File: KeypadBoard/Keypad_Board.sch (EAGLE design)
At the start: 34 parts, among them Q1 4.3A/20V/54mΩ, U1 ESP32-WROOM-32E_(16MB), U2 LTC1730ES8-4.2#TRPBF

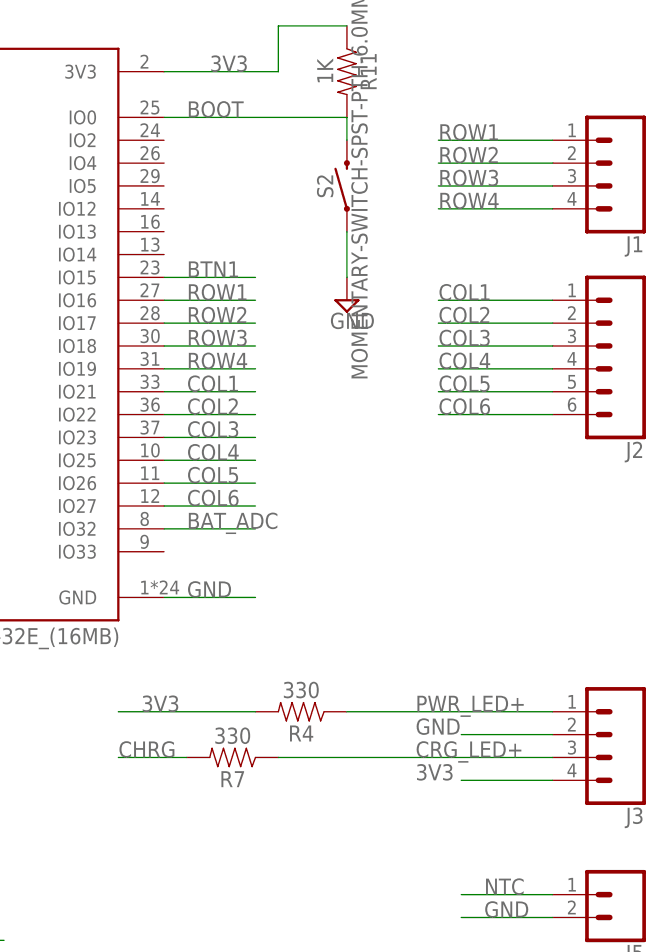
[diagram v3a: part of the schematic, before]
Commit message: Updated board for connection of a Micro SD Card module
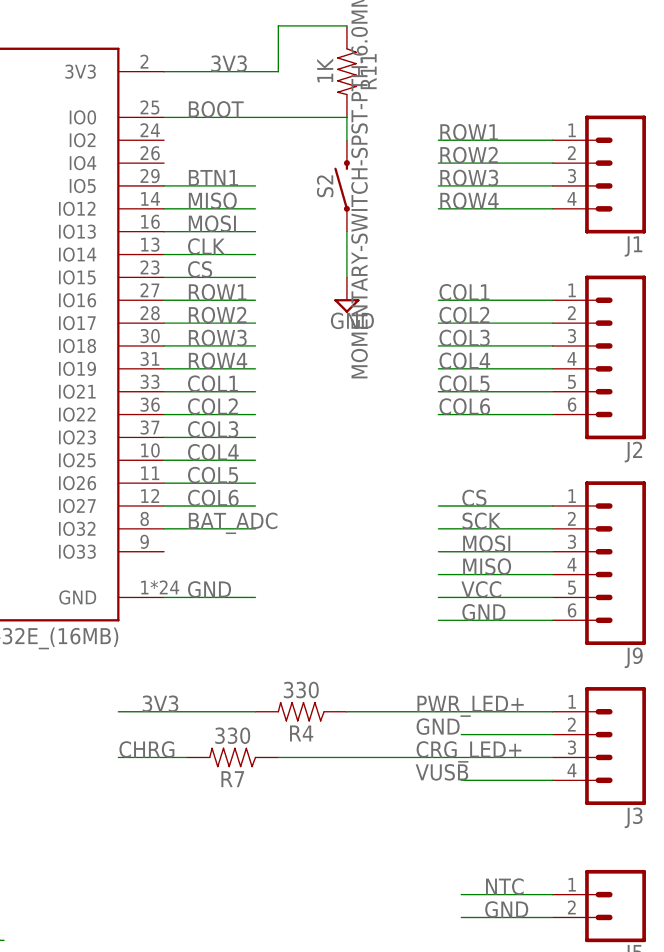
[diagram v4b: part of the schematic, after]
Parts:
- added J9: (no value), SparkFun-Connectors:CONN_06LOCK
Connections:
- new net CLK: U1.IO14
- new net CS: J9.1, U1.IO15
- new net MISO: J9.4, U1.IO12
- new net MOSI: J9.3, U1.IO13
- new net SCK: J9.2
- net 3V3: no longer J3.4
- net BTN1: now also U1.IO5; no longer U1.IO15
- net GND: now also J9.6
- net VCC: now also J9.5
- net VUSB: now also J3.4
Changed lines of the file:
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@@
 <part name="R13" library="SparkFun-Resistors" library_urn="urn:adsk.eagle:library:532" deviceset="0.22OHM" device="-0805-1/4W-1%" package3d_urn="urn:adsk.eagle:package:39651/1" value="120K"/>
 <part name="SUPPLY11" library="supply2" library_urn="urn:adsk.eagle:library:372" deviceset="GND" device=""/>
+<part name="J9" library="SparkFun-Connectors" library_urn="urn:adsk.eagle:library:513" deviceset="CONN_06" device="LOCK" package3d_urn="urn:adsk.eagle:package:38002/1"/>
 </parts>
 <sheets>
@@
 <attribute name="VALUE" x="112.395" y="90.805" size="1.778" layer="96"/>
 </instance>
+<instance part="J9" gate="G$1" x="322.58" y="101.6" smashed="yes" rot="R180">
+<attribute name="VALUE" x="327.66" y="111.506" size="1.778" layer="96" font="vector" rot="R180"/>
+<attribute name="NAME" x="327.66" y="90.932" size="1.778" layer="95" font="vector" rot="R180"/>
+</instance>
 </instances>
 <busses>
@@
 <pinref part="R12" gate="G$1" pin="2"/>
 <wire x1="114.3" y1="96.52" x2="114.3" y2="99.06" width="0.1524" layer="91"/>
+</segment>
+<segment>
+<pinref part="J9" gate="G$1" pin="6"/>
+<wire x1="317.5" y1="93.98" x2="304.8" y2="93.98" width="0.1524" layer="91"/>
+<label x="307.34" y="93.98" size="1.778" layer="95"/>
 </segment>
 </net>
@@
 <wire x1="76.2" y1="99.06" x2="88.9" y2="99.06" width="0.1524" layer="91"/>
 <label x="81.28" y="99.06" size="1.778" layer="95"/>
+</segment>
+<segment>
+<pinref part="J9" gate="G$1" pin="5"/>
+<wire x1="317.5" y1="96.52" x2="304.8" y2="96.52" width="0.1524" layer="91"/>
+<label x="307.34" y="96.52" size="1.778" layer="95"/>
 </segment>
 </net>
@@
 <label x="81.28" y="129.54" size="1.778" layer="95"/>
 </segment>
+<segment>
+<pinref part="J3" gate="G$1" pin="4"/>
+<wire x1="317.5" y1="76.2" x2="307.34" y2="76.2" width="0.1524" layer="91"/>
+<label x="302.26" y="76.2" size="1.778" layer="95"/>
+</segment>
 </net>
 <net name="3V3" class="0">
@@
 <label x="307.34" y="50.8" size="1.778" layer="95"/>
 </segment>
-<segment>
-<pinref part="J3" gate="G$1" pin="4"/>
-<wire x1="317.5" y1="76.2" x2="307.34" y2="76.2" width="0.1524" layer="91"/>
-<label x="302.26" y="76.2" size="1.778" layer="95"/>
-</segment>
 </net>
 <net name="N$9" class="0">
@@
 </segment>
 <segment>
-<pinref part="U1" gate="G$1" pin="IO15"/>
-<wire x1="274.32" y1="132.08" x2="284.48" y2="132.08" width="0.1524" layer="91"/>
-<label x="276.86" y="132.08" size="1.778" layer="95"/>
+<pinref part="U1" gate="G$1" pin="IO5"/>
+<wire x1="274.32" y1="142.24" x2="284.48" y2="142.24" width="0.1524" layer="91"/>
+<label x="276.86" y="142.24" size="1.778" layer="95"/>
 </segment>
 </net>
@@
 </segment>
 </net>
+<net name="MISO" class="0">
+<segment>
+<pinref part="U1" gate="G$1" pin="IO12"/>
+<wire x1="274.32" y1="139.7" x2="284.48" y2="139.7" width="0.1524" layer="91"/>
+<label x="276.86" y="139.7" size="1.778" layer="95"/>
+</segment>
+<segment>
+<pinref part="J9" gate="G$1" pin="4"/>
+<wire x1="317.5" y1="99.06" x2="304.8" y2="99.06" width="0.1524" layer="91"/>
+<label x="307.34" y="99.06" size="1.778" layer="95"/>
+</segment>
+</net>
+<net name="MOSI" class="0">
+<segment>
+<pinref part="U1" gate="G$1" pin="IO13"/>
+<wire x1="274.32" y1="137.16" x2="284.48" y2="137.16" width="0.1524" layer="91"/>
+<label x="276.86" y="137.16" size="1.778" layer="95"/>
+</segment>
+<segment>
+<pinref part="J9" gate="G$1" pin="3"/>
+<wire x1="317.5" y1="101.6" x2="304.8" y2="101.6" width="0.1524" layer="91"/>
+<label x="307.34" y="101.6" size="1.778" layer="95"/>
+</segment>
+</net>
+<net name="CLK" class="0">
+<segment>
+<pinref part="U1" gate="G$1" pin="IO14"/>
+<wire x1="274.32" y1="134.62" x2="284.48" y2="134.62" width="0.1524" layer="91"/>
+<label x="276.86" y="134.62" size="1.778" layer="95"/>
+</segment>
+</net>
+<net name="CS" class="0">
+<segment>
+<pinref part="U1" gate="G$1" pin="IO15"/>
+<wire x1="274.32" y1="132.08" x2="284.48" y2="132.08" width="0.1524" layer="91"/>
+<label x="276.86" y="132.08" size="1.778" layer="95"/>
+</segment>
+<segment>
+<pinref part="J9" gate="G$1" pin="1"/>
+<wire x1="317.5" y1="106.68" x2="304.8" y2="106.68" width="0.1524" layer="91"/>
+<label x="307.34" y="106.68" size="1.778" layer="95"/>
+</segment>
+</net>
+<net name="SCK" class="0">
+<segment>
+<pinref part="J9" gate="G$1" pin="2"/>
+<wire x1="317.5" y1="104.14" x2="304.8" y2="104.14" width="0.1524" layer="91"/>
+<label x="307.34" y="104.14" size="1.778" layer="95"/>
+</segment>
+</net>

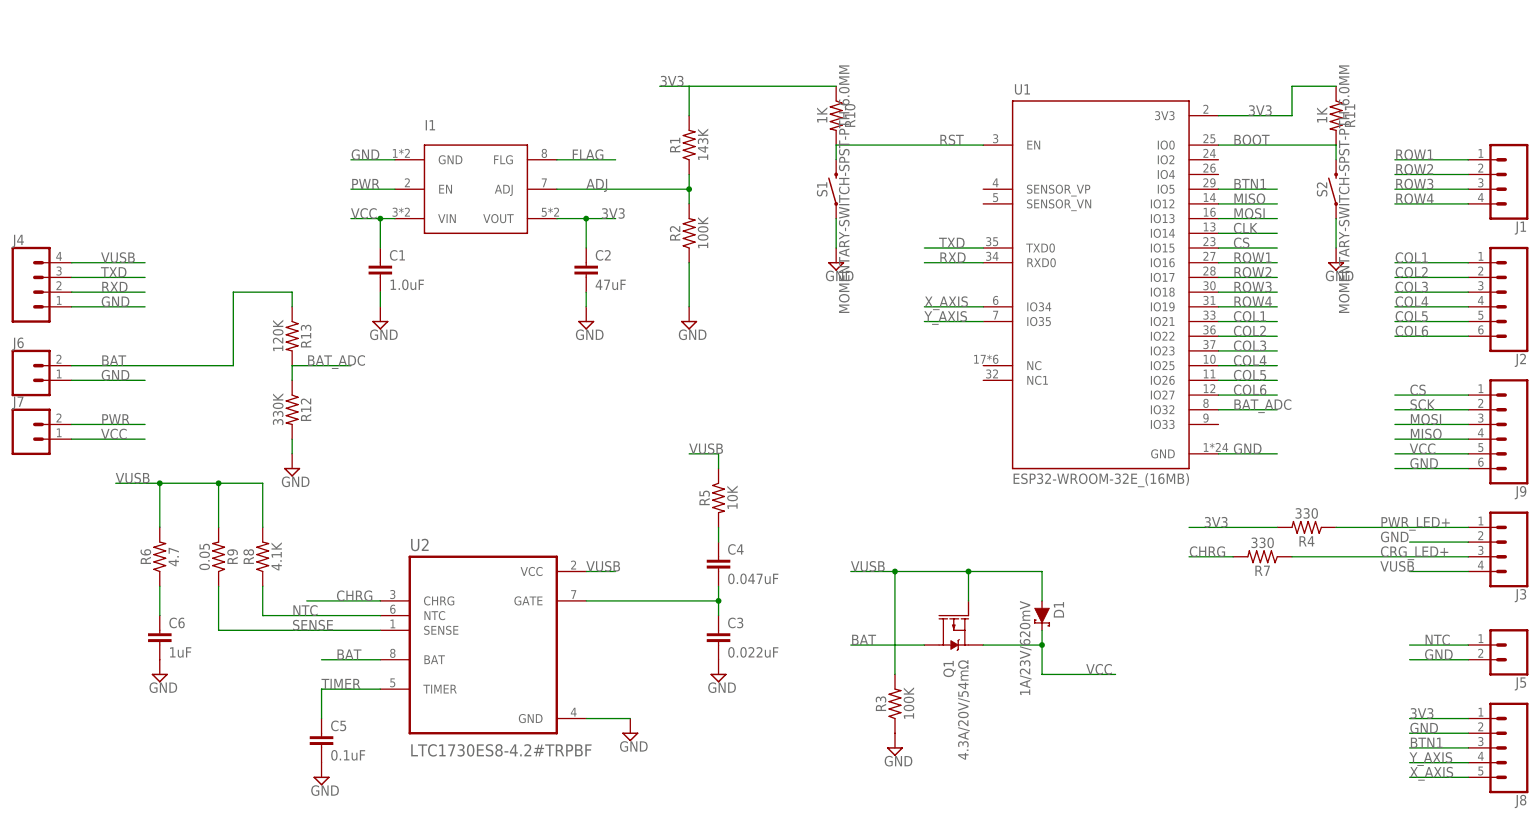
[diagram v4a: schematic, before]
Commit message: Board V4 - integrated battery holder, SD Breakout, mode LED's
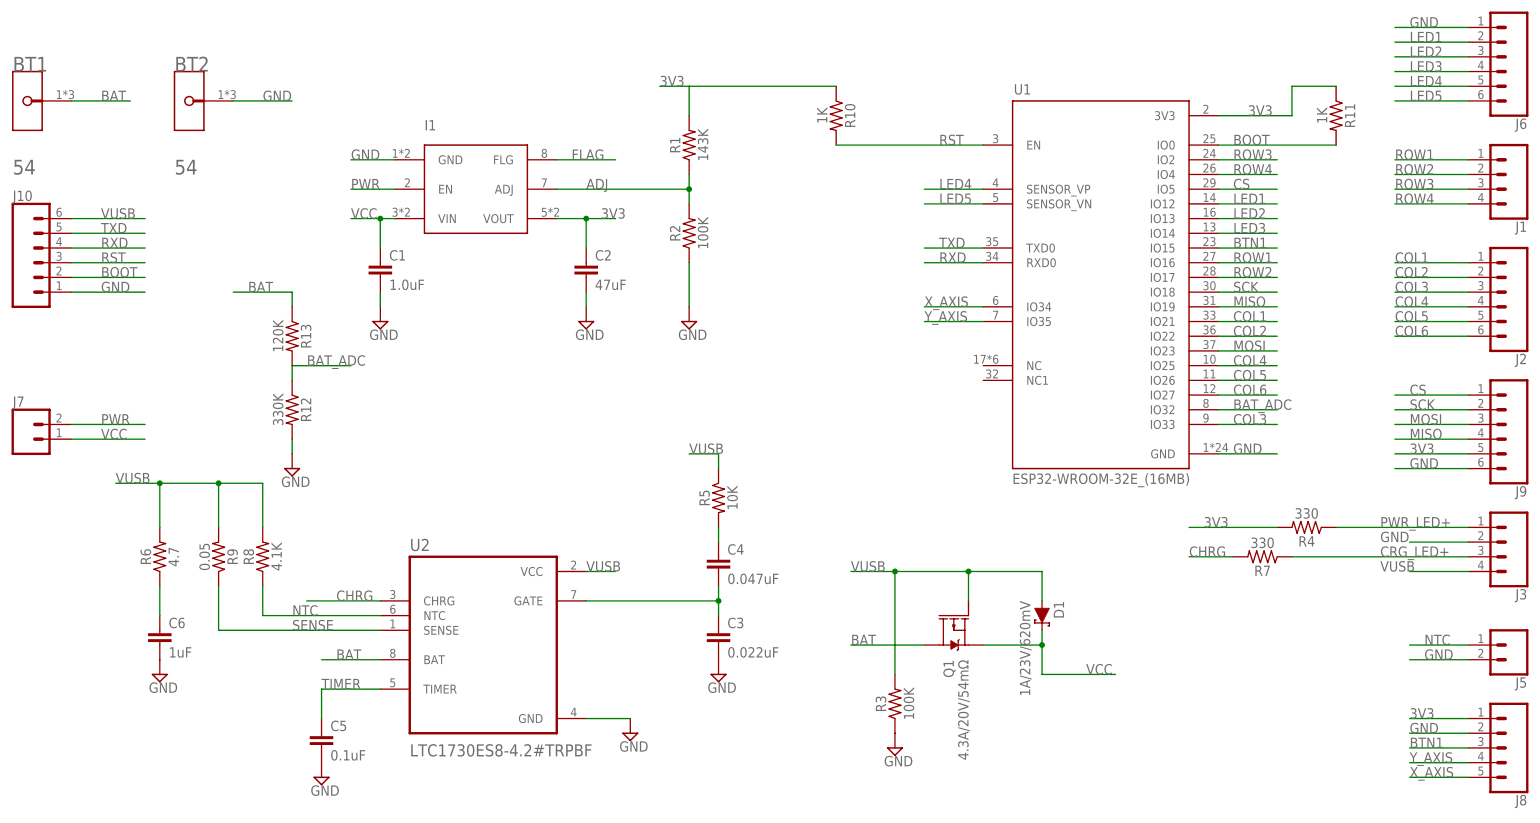
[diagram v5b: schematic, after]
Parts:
- removed J4: (no value), SparkFun-Connectors:CONN_04
- removed S1, S2: MOMENTARY-SWITCH-SPST-PTH-6.0MM, SparkFun-Switches:MOMENTARY-SWITCH-SPST-PTH-6.0MM
- added BT1, BT2: KEYSTONE_54KEYSTONE_54_0_0, Keystone - 54:KEYSTONE_54KEYSTONE_54_0_0
- added J10: (no value), SparkFun-Connectors:CONN_06LOCK
- J6: device SparkFun-Connectors:CONN_02 -> SparkFun-Connectors:CONN_06LOCK
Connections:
- removed net CLK: U1.IO14
- new net LED1: J6.2, U1.IO12
- new net LED2: J6.3, U1.IO13
- new net LED3: J6.4, U1.IO14
- new net LED4: J6.5, U1.SENSOR_VP
- new net LED5: J6.6, U1.SENSOR_VN
- net 3V3: now also J9.5
- net BAT: now also BT1.1; no longer J6.2
- net BOOT: now also J10.2; no longer S2.2
- net BTN1: now also U1.IO15; no longer U1.IO5
- net COL3: now also U1.IO33; no longer U1.IO23
- net CS: now also U1.IO5; no longer U1.IO15
- net GND: now also BT2.1, J10.1; no longer J4.1, S1.1, S2.1
- net MISO: now also U1.IO19; no longer U1.IO12
- net MOSI: now also U1.IO23; no longer U1.IO13
- net ROW3: now also U1.IO2; no longer U1.IO18
- net ROW4: now also U1.IO4; no longer U1.IO19
- net RST: now also J10.3; no longer S1.2
- net RXD: now also J10.4; no longer J4.2
- net SCK: now also U1.IO18
- net TXD: now also J10.5; no longer J4.3
- net VCC: no longer J9.5
- net VUSB: now also J10.6; no longer J4.4
